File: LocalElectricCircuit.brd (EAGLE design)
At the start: 160 x 100 mm, 53 parts, among them IC1 PIC32MX360F512L, J1 Prog. Port, U1 ADS1118, U2 ADS1118, X2 MALE_VGA

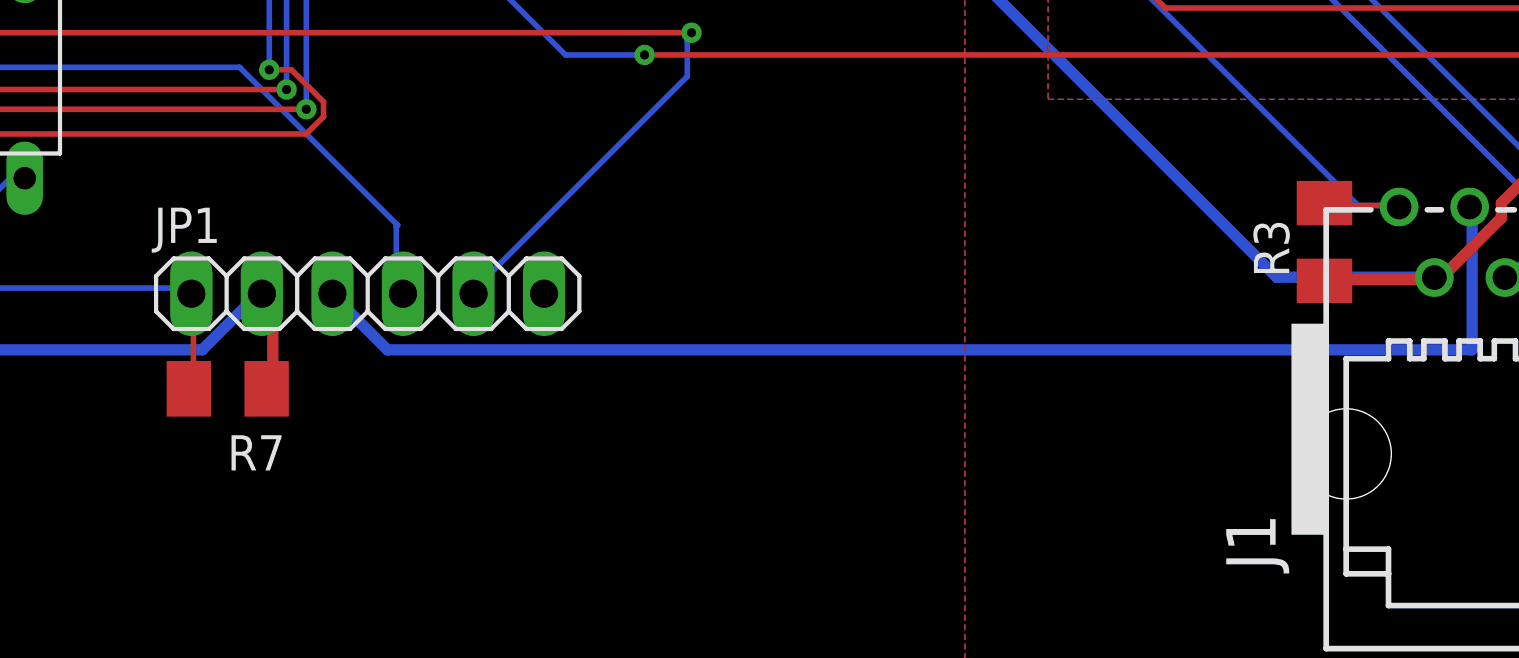
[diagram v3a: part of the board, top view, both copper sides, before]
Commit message: Fixed planes, resistor collision
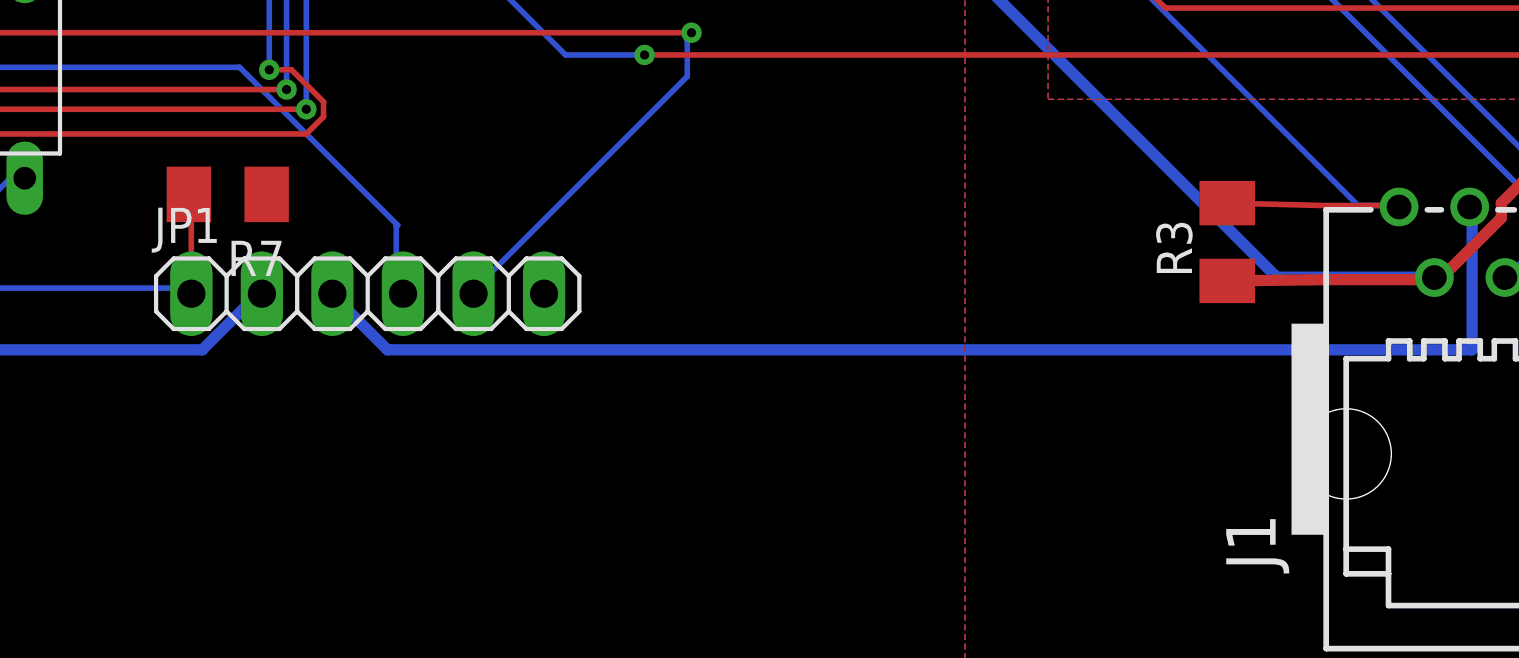
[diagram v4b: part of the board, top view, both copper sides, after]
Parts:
- moved R7 7.00 mm to (87.0, -27.4)
- moved R3 3.50 mm to (122.9, -29.1)
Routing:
- net +3V3: track 472.2 -> 525.2 mm, vias 26 -> 32
- net +3V1: track 49.5 -> 0.00 mm, vias 6 -> 0
- net PIC16_3V3: track 57.4 -> 53.7 mm
- net !MCLR: track 81.2 -> 84.6 mm
- added copper zone on layer 1, net PIC16_3V3
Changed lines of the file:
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@@
 <setting verticaltext="up"/>
 </settings>
-<grid distance="0.5" unitdist="mm" unit="mm" style="lines" multiple="1" display="yes" altdistance="0.1" altunitdist="mm" altunit="mm"/>
+<grid distance="10" unitdist="mil" unit="mil" style="dots" multiple="1" display="yes" altdistance="5" altunitdist="mil" altunit="mil"/>
 <layers>
 <layer number="1" name="Top" color="4" fill="1" visible="yes" active="yes"/>
@@
 <element name="C7" library="resistor" package="C1206" value="0.1uF" x="62.5" y="16.4" smashed="yes" rot="MR0"/>
 <element name="J1" library="con-amp" package="520258-3" value="Prog. Port" x="132.31" y="-35.878"/>
-<element name="R3" library="rcl" package="M1206" value="50k" x="126.448" y="-29.138" smashed="yes" rot="R90">
-<attribute name="NAME" x="125.178" y="-30.408" size="1.27" layer="25" rot="R90"/>
-<attribute name="VALUE" x="125.133634375" y="-27.707121875" size="1.27" layer="27" rot="R90"/>
+<element name="R3" library="rcl" package="M1206" value="50k" x="122.948" y="-29.138" smashed="yes" rot="R90">
+<attribute name="NAME" x="121.678" y="-30.408" size="1.27" layer="25" rot="R90"/>
+<attribute name="VALUE" x="121.633634375" y="-27.707121875" size="1.27" layer="27" rot="R90"/>
 </element>
 <element name="J2" library="19inch_VG96KB" package="VG96KB" value="" x="0" y="0"/>
@@
 <attribute name="VALUE" x="67.826" y="-31.462" size="1.27" layer="27" rot="R180"/>
 </element>
-<element name="R7" library="rcl" package="M1206" value="50k" x="86.96" y="-34.424" smashed="yes" rot="R180">
-<attribute name="NAME" x="89.03" y="-36.094" size="1.27" layer="25" rot="R180"/>
-<attribute name="VALUE" x="89.03" y="-37.884" size="1.27" layer="27" rot="R180"/>
+<element name="R7" library="rcl" package="M1206" value="50k" x="86.96" y="-27.424" smashed="yes" rot="R180">
+<attribute name="NAME" x="89.03" y="-29.094" size="1.27" layer="25" rot="R180"/>
+<attribute name="VALUE" x="89.03" y="-30.884" size="1.27" layer="27" rot="R180"/>
 </element>
 <element name="C12" library="resistor" package="C1206" value="0.01uF" x="74.3" y="18.2" smashed="yes" rot="MR270"/>
@@
 <wire x1="152.1079" y1="39.3827" x2="152.126" y2="39.37" width="0.4064" layer="1"/>
 <wire x1="130.3274" y1="-30.4927" x2="126.5047" y2="-30.4927" width="0.4064" layer="1"/>
-<wire x1="126.5047" y1="-30.4927" x2="126.448" y2="-30.538" width="0.4064" layer="1"/>
+<wire x1="126.5047" y1="-30.4927" x2="122.948" y2="-30.538" width="0.4064" layer="1"/>
 <wire x1="130.3274" y1="-30.4927" x2="130.405" y2="-30.417" width="0.4064" layer="1"/>
 <wire x1="70.7644" y1="16.8021" x2="70.7644" y2="14.6685" width="0.4064" layer="16"/>
@@
 <vertex x="113.5" y="35"/>
 </polygon>
-<polygon width="0.4064" layer="1">
-<vertex x="40.5" y="-14.5"/>
-<vertex x="40.5" y="-44.5"/>
-<vertex x="113.5" y="-44.5"/>
-<vertex x="113.5" y="-14.5"/>
-</polygon>
 <wire x1="152.1968" y1="38.4048" x2="152.1968" y2="39.3032" width="0.6096" layer="1"/>
 <wire x1="152.1968" y1="39.3032" x2="152" y2="39.5" width="0.6096" layer="1"/>
@@
 <contactref element="X2" pad="8"/>
 <contactref element="X2" pad="15"/>
+<via x="55" y="26.5" extent="1-16" drill="0.3302"/>
+<via x="55" y="28" extent="1-16" drill="0.3302"/>
+<via x="55" y="29.5" extent="1-16" drill="0.3302"/>
+<via x="40.5" y="26.5" extent="1-16" drill="0.3302"/>
+<via x="40.5" y="28" extent="1-16" drill="0.3302"/>
+<via x="40.5" y="29.5" extent="1-16" drill="0.3302"/>
+<wire x1="40.5" y1="26.5" x2="40.5" y2="28" width="1.6256" layer="16"/>
+<wire x1="40.5" y1="28" x2="40.5" y2="29.5" width="1.6256" layer="16"/>
+<wire x1="55" y1="26.5" x2="55" y2="28" width="1.6256" layer="16"/>
+<wire x1="55" y1="28" x2="55" y2="29.5" width="1.6256" layer="16"/>
+<wire x1="55" y1="29.5" x2="40.5" y2="29.5" width="1.6256" layer="16"/>
+<wire x1="55" y1="28" x2="40.5" y2="28" width="1.6256" layer="16"/>
+<wire x1="55" y1="26.5" x2="40.5" y2="26.5" width="1.6256" layer="16"/>
 </signal>
 <signal name="GND_3V3" class="1">
@@
 <via x="68.8" y="1.6" extent="1-16" drill="0.3302" shape="octagon"/>
 <wire x1="129.0828" y1="-27.8257" x2="126.5047" y2="-27.8257" width="0.2032" layer="1"/>
-<wire x1="126.5047" y1="-27.8257" x2="126.448" y2="-27.738" width="0.2032" layer="1"/>
+<wire x1="126.5047" y1="-27.8257" x2="122.948" y2="-27.738" width="0.2032" layer="1"/>
 <wire x1="129.0828" y1="-27.8257" x2="129.135" y2="-27.877" width="0.2032" layer="1"/>
 <wire x1="69.4309" y1="1.6002" x2="68.8975" y2="1.6002" width="0.2032" layer="1"/>
@@
 <contactref element="R7" pad="2"/>
 <contactref element="JP1" pad="1"/>
-<wire x1="85.725" y1="-31.115" x2="85.725" y2="-34.29" width="0.2032" layer="1"/>
-<wire x1="85.725" y1="-34.29" x2="85.56" y2="-34.424" width="0.2032" layer="1"/>
-<wire x1="85.725" y1="-31.115" x2="85.65" y2="-31" width="0.2032" layer="1"/>
 <wire x1="64.135" y1="-29.21" x2="64.135" y2="-26.9875" width="0.2032" layer="1"/>
 <wire x1="65.7225" y1="-30.7975" x2="64.135" y2="-29.21" width="0.2032" layer="16"/>
@@
 <wire x1="85.4075" y1="-30.7975" x2="85.65" y2="-31" width="0.2032" layer="16"/>
 <via x="64.135" y="-29.21" extent="1-16" drill="0.3302"/>
+<wire x1="85.56" y1="-27.424" x2="85.65" y2="-27.424" width="0.2032" layer="1"/>
+<wire x1="85.65" y1="-27.424" x2="85.65" y2="-31" width="0.2032" layer="1"/>
 </signal>
 <signal name="PBUS5">
@@
 <wire x1="50.8" y1="-32.0964" x2="50.7364" y2="-32.0328" width="0.4064" layer="1"/>
 <contactref element="JP1" pad="2"/>
-<wire x1="88.5825" y1="-31.4325" x2="88.5825" y2="-34.29" width="0.4064" layer="1"/>
-<wire x1="88.265" y1="-31.115" x2="88.5825" y2="-31.4325" width="0.4064" layer="1"/>
-<wire x1="88.5825" y1="-34.29" x2="88.36" y2="-34.424" width="0.4064" layer="1"/>
-<wire x1="88.265" y1="-31.115" x2="88.19" y2="-31" width="0.4064" layer="1"/>
 <wire x1="86.0425" y1="-33.02" x2="87.9475" y2="-31.115" width="0.4064" layer="16"/>
 <wire x1="51.7525" y1="-33.02" x2="86.0425" y2="-33.02" width="0.4064" layer="16"/>
@@
 <wire x1="87.9475" y1="-31.115" x2="88.19" y2="-31" width="0.4064" layer="16"/>
 <wire x1="50.8" y1="-32.0675" x2="50.7364" y2="-32.0328" width="0.4064" layer="16"/>
+<polygon width="0.4064" layer="1">
+<vertex x="40.5" y="-14.5"/>
+<vertex x="40.5" y="-44.5"/>
+<vertex x="113.5" y="-44.5"/>
+<vertex x="113.5" y="-14.5"/>
+</polygon>
 </signal>
 <signal name="EXT_TEMP">
@@
 <wire x1="137.1727" y1="-19.558" x2="137.1692" y2="-19.6276" width="0.2032" layer="1"/>
 </signal>
-<signal name="+3V1" class="1">
-<via x="55" y="26.5" extent="1-16" drill="0.3302"/>
-<via x="55" y="28" extent="1-16" drill="0.3302"/>
-<via x="55" y="29.5" extent="1-16" drill="0.3302"/>
-<via x="40.5" y="26.5" extent="1-16" drill="0.3302"/>
-<via x="40.5" y="28" extent="1-16" drill="0.3302"/>
-<via x="40.5" y="29.5" extent="1-16" drill="0.3302"/>
-<wire x1="40.5" y1="26.5" x2="40.5" y2="28" width="1.6256" layer="16"/>
-<wire x1="40.5" y1="28" x2="40.5" y2="29.5" width="1.6256" layer="16"/>
-<wire x1="55" y1="26.5" x2="55" y2="28" width="1.6256" layer="16"/>
-<wire x1="55" y1="28" x2="55" y2="29.5" width="1.6256" layer="16"/>
-<wire x1="55" y1="29.5" x2="40.5" y2="29.5" width="1.6256" layer="16"/>
-<wire x1="55" y1="28" x2="40.5" y2="28" width="1.6256" layer="16"/>
-<wire x1="55" y1="26.5" x2="40.5" y2="26.5" width="1.6256" layer="16"/>
-</signal>
 </signals>

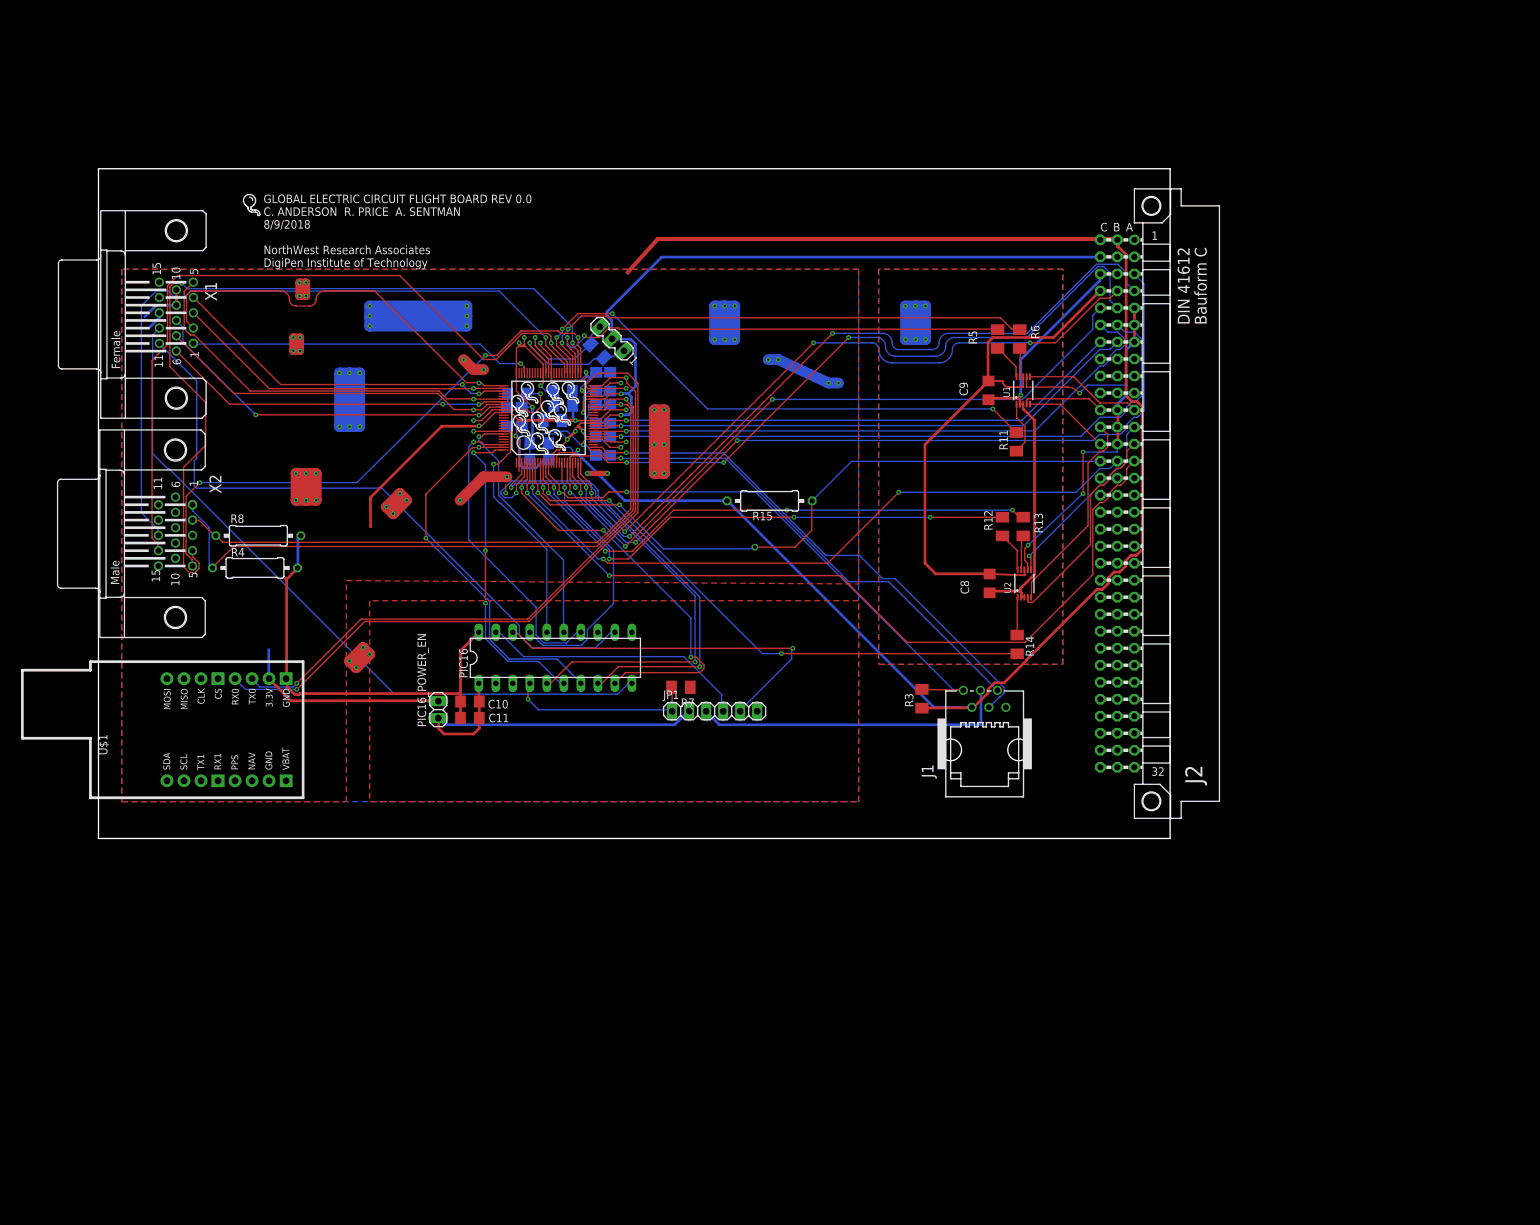
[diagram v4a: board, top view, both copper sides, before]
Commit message: Update silk screen with REv 1.0 and date Added fan out for all PIC pins Began on fan out for ADC pins ETC.
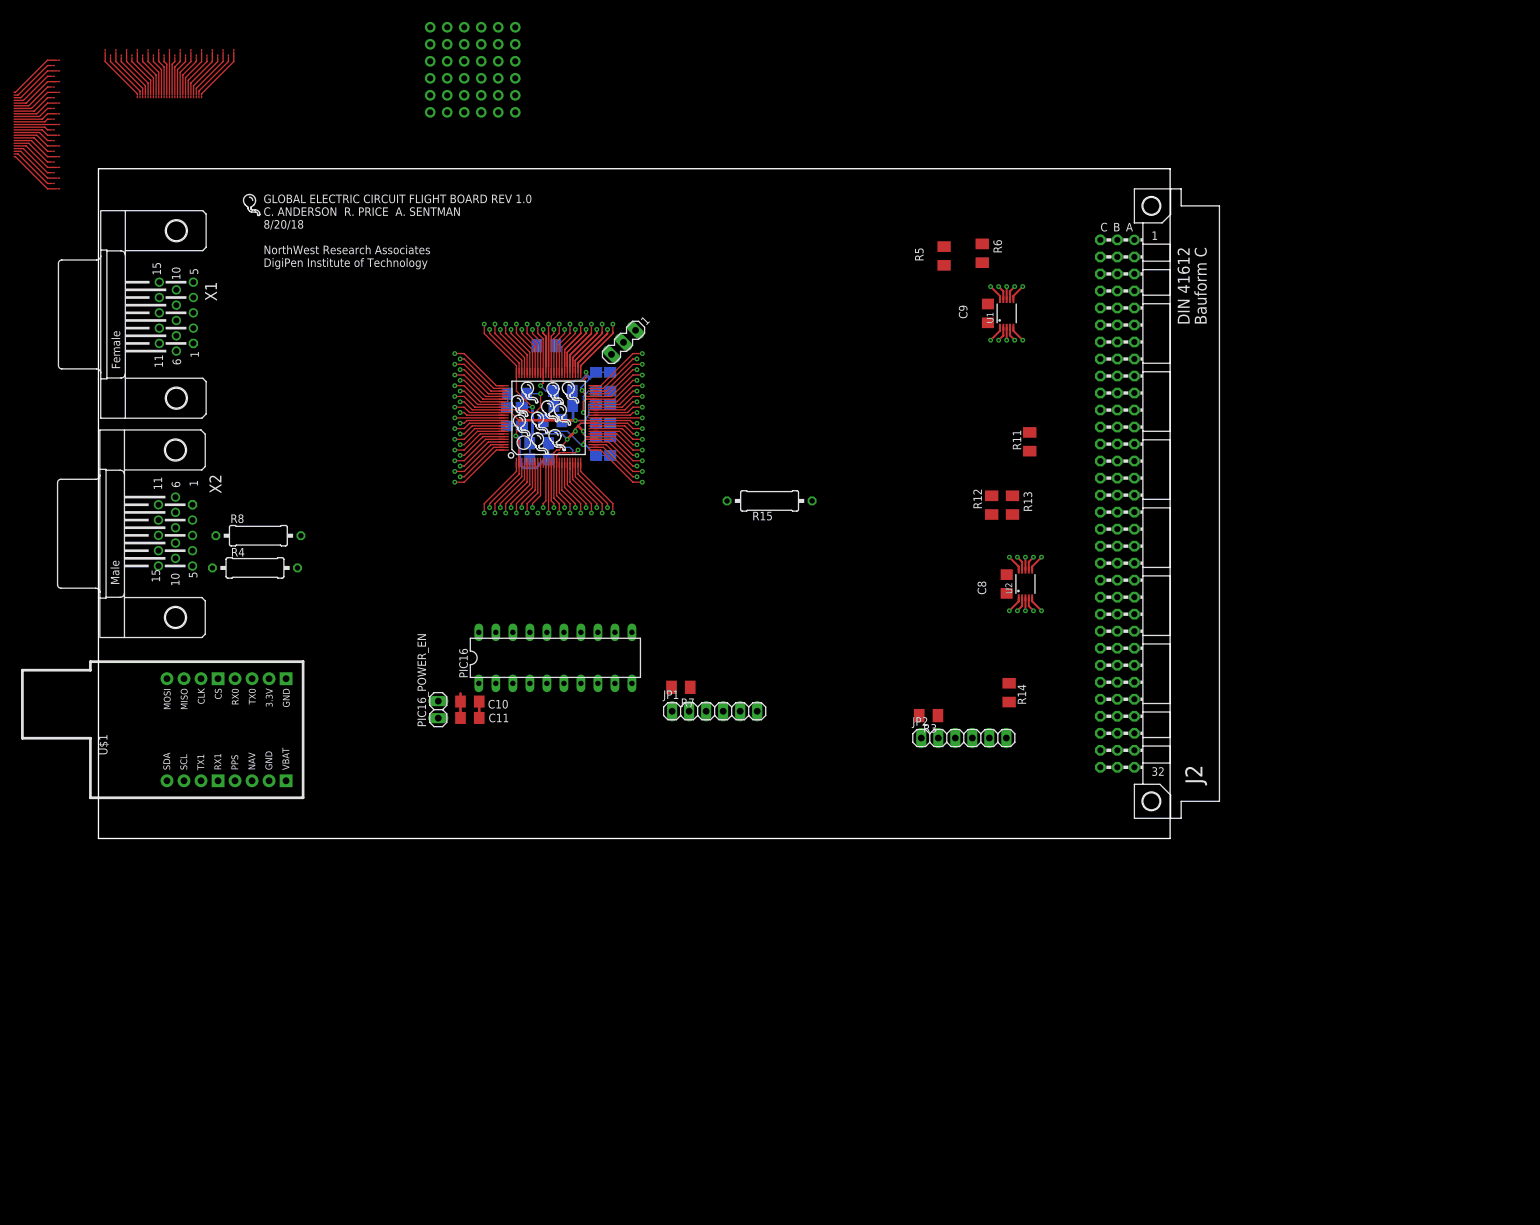
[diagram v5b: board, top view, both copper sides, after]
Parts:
- removed J1: Prog. Port, con-amp:520258-3
- added JP2: (no value), pinhead:1X06
- R3, R7: value 50k -> 10k
- moved R5 14.8 mm to (126.2, 37.0)
- moved R6 14.0 mm to (132.0, 37.4)
- moved U1 11.8 mm to (135.6, 28.4)
- moved C9 11.5 mm to (132.8, 28.4)
- moved R1 7.64 mm to (66.9, 23.6), turned to 0 degrees
- moved R14 7.30 mm to (136.0, -28.2)
- moved R12 3.58 mm to (133.4, -0.23)
- moved R13 3.58 mm to (136.5, -0.23)
- moved R3 2.70 mm to (123.9, -31.7), turned to 180 degrees
- moved C8 2.55 mm to (135.6, -12.0)
- moved R11 2.00 mm to (139.0, 9.23)
- moved SV1 1.80 mm to (78.4, 24.1), turned to 225 degrees
- moved U2 0.18 mm to (138.4, -12.0)
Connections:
- net !MCLR: now also JP2.1; no longer J1.1
- net +3V3: now also JP2.2; no longer J1.2
- net GND_3V3: now also JP2.3; no longer J1.3
- net PGEC2: now also JP2.5; no longer J1.5
- net PGED2: now also JP2.4; no longer J1.4
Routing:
- net +3V3: track 525.2 -> 112.2 mm, vias 32 -> 9
- net GND_3V3: track 396.4 -> 111.6 mm, vias 45 -> 11
- net CHARGE_PROBE_0: track 122.7 -> 7.86 mm, vias 2 -> 1
- net TEMP_3: track 122.0 -> 8.19 mm, vias 3 -> 1
- net U1RX: track 121.6 -> 8.32 mm, vias 2 -> 1
- net PIC16_TX: track 106.2 -> 0.00 mm
- net I2C_SDA: track 112.3 -> 7.66 mm
- net TEMP_2: track 111.4 -> 8.52 mm, vias 3 -> 1
- net I2C_SCL: track 106.6 -> 8.29 mm
- net PIC16_RX: track 98.3 -> 0.00 mm
- net U2RX: track 106.1 -> 8.32 mm, vias 2 -> 1
- net I_1_L: track 106.5 -> 8.94 mm, vias 4 -> 1
- net +5V: track 101.4 -> 3.90 mm, vias 6 -> 0
- net I_1_H: track 103.2 -> 7.86 mm, vias 3 -> 1
- net TEMP_1: track 103.9 -> 9.49 mm, vias 4 -> 1
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- removed copper zone on layer 1, net +3V3
- removed copper zone on layer 1, net +5V
- removed copper zone on layer 16, net GND
- removed copper zone on layer 16, net GND_3V3
- removed copper zone on layer 1, net PIC16_3V3
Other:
- board text added: "GLOBAL ELECTRIC CIRCUIT FLIGHT BOARD REV 1.0 C. ANDERSON R. PRICE A. SENTMAN 8/20/18 NorthWest Research Associates DigiPen Institute of Technology"
- board text removed: "GLOBAL ELECTRIC CIRCUIT FLIGHT BOARD REV 0.0 C. ANDERSON R. PRICE A. SENTMAN 8/9/2018 NorthWest Research Associates DigiPen Institute of Technology"
